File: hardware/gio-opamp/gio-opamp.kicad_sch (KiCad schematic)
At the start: 25 parts, among them J1 PJ3001F, J2 PJ3001F, U1 TL072, U2 MCP3208, U3 DAC8552, U4 XIAO-RP2350-DIP

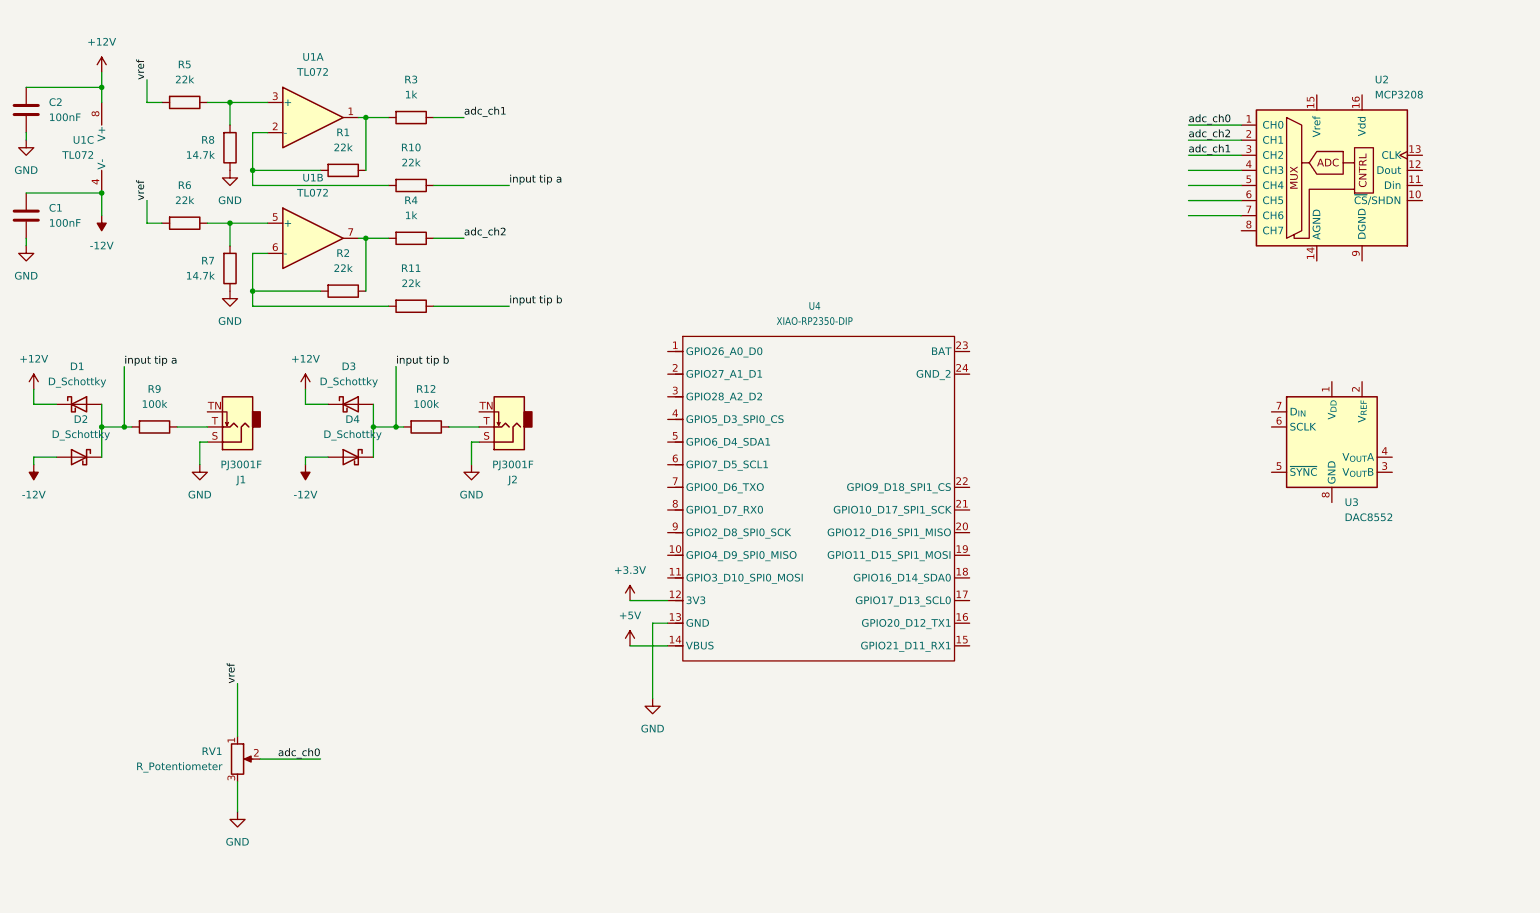
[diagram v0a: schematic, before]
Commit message: KiCad input stage: review-driven schematic refinements
Updates from the 2026-05-03 schematic review:

- Net `input tip a/b` renamed to `clamp_a/clamp_b` (more accurate --
  it's the protection node *after* R_series, not the jack tip itself).
- Local 100nF decoupling cap (C5) added directly across U1 V+/V- pins
  for fast op-amp transient response, in addition to the existing
  bulk caps on the +/-12V rails (C1/C2).
- Per-channel 100nF filter caps (C3/C4) on each bias-divider node to
  knock down any high-frequency noise riding on VREF before it reaches
  the op-amp non-inverting inputs.
- Schottky clamps switched from generic D_Schottky symbol to the
  BAT54S 3-pin series-pair (A=pin1, K=pin2, COM=pin3 on signal node).
  One part replaces two BAT43s per channel for the production PCB.

Schematic still input-stage-only; output stage / VREF / MCU coming
in subsequent edits.

Co-Authored-By: Claude Opus 4.7 (1M context) <noreply@anthropic.com>
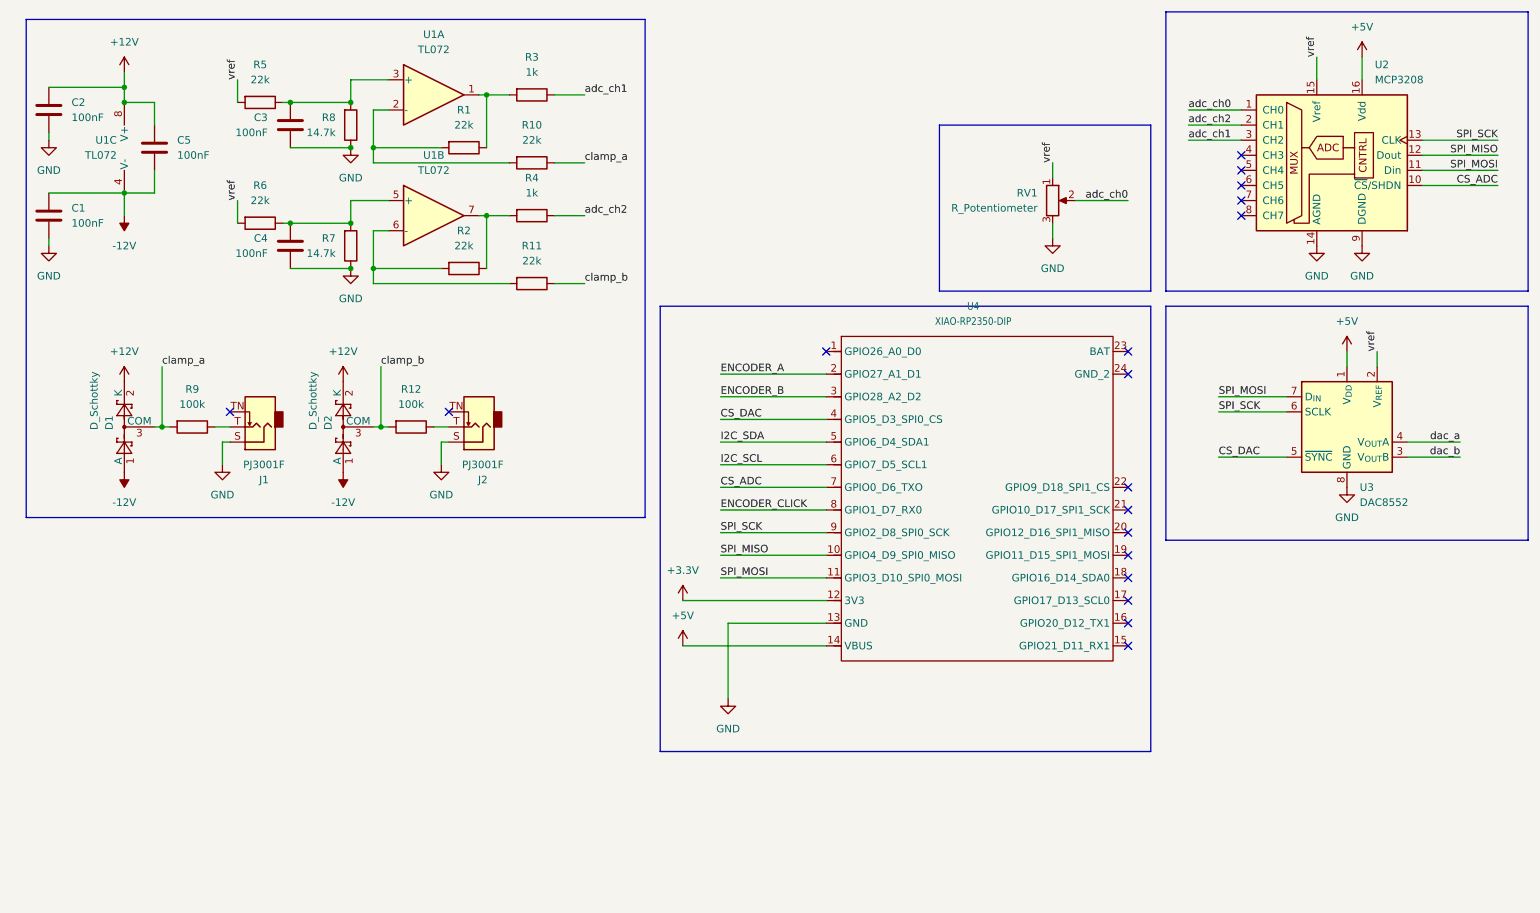
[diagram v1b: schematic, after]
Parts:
- removed D2, D3, D4: D_Schottky, symbol Device:D_Schottky
- added C3, C4, C5: 100nF, symbol Device:C
- added D2: D_Schottky, Package_TO_SOT_SMD:SOT-23, symbol Diode:BAT54S
- D1: footprint (none) -> Package_TO_SOT_SMD:SOT-23; symbol Device:D_Schottky -> Diode:BAT54S
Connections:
- net +12V: now also D1.2 (K), C5.1, D2.2 (K); no longer D1.1 (K)
- net +5V: now also U2.16 (Vdd), U3.1 (V_{DD})
- net -12V: now also D1.1 (A), C5.2, D2.1 (A)
- net GND: now also U2.14 (AGND), U2.9 (DGND), U3.8 (GND), C3.2, C4.2
- net vref: now also U2.15 (Vref), U3.2 (V_{REF})
- net at R6.1, R7.2, U1.5 (+): now also C4.1
- net at R5.1, R8.2, U1.3 (+): now also C3.1
- net SPI_MISO: now reaches U4.10 (GPIO4_D9_SPI0_MISO)
- net SPI_MISO: now also U2.12 (Dout)
- net SPI_MOSI: now reaches U4.11 (GPIO3_D10_SPI0_MOSI)
- net SPI_MOSI: now also U2.11 (Din), U3.7 (D_{IN})
- net ENCODER_A: now reaches U4.2 (GPIO27_A1_D1)
- net ENCODER_B: now reaches U4.3 (GPIO28_A2_D2)
- net CS_DAC: now reaches U4.4 (GPIO5_D3_SPI0_CS)
- net CS_DAC: now also U3.5 (~{SYNC})
- net I2C_SDA: now reaches U4.5 (GPIO6_D4_SDA1)
- net I2C_SCL: now reaches U4.6 (GPIO7_D5_SCL1)
- net CS_ADC: now reaches U4.7 (GPIO0_D6_TXO)
- net CS_ADC: now also U2.10 (~{CS}/SHDN)
- net ENCODER_CLICK: now reaches U4.8 (GPIO1_D7_RX0)
- net SPI_SCK: now reaches U4.9 (GPIO2_D8_SPI0_SCK)
- net SPI_SCK: now also U2.13 (CLK), U3.6 (SCLK)
- net dac_b: now reaches U3.3 (V_{OUT}B)
- net dac_a: now reaches U3.4 (V_{OUT}A)
- net input tip a renamed clamp_a
- net clamp_a: now also D1.3 (COM); no longer D1.2 (A)
- net input tip b renamed clamp_b
- net clamp_b: now also D2.3 (COM)
- no-connect marks 0 -> 18
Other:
- moved on the sheet: C1, C2, J1, R1, R10, R11, R2, R3, R4, R5, R6, R7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

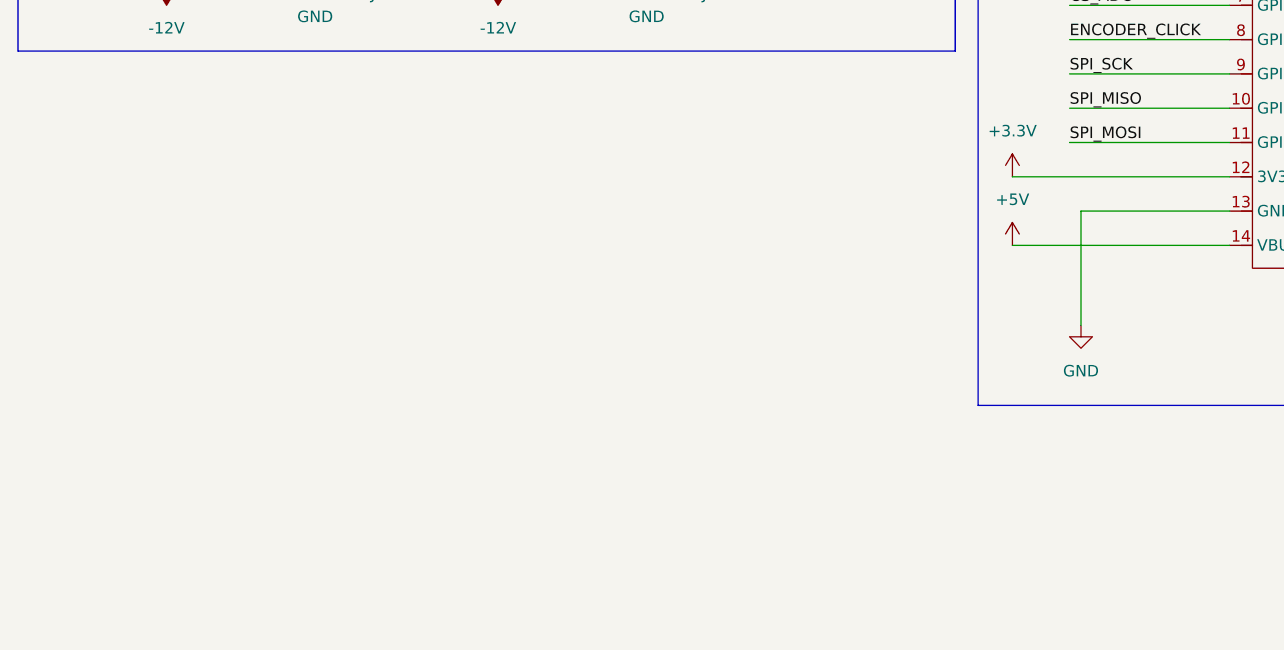
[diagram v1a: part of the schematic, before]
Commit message: KiCad: generate output op-amp stage (U5) via Python script
Adds the full output op-amp stage to the schematic by translating the
input op-amp section by +100 in Y and remapping references, values,
and net labels for the output topology.

Components added (all in y range 100-160 of the schematic):
  U5         TL072 (3 unit instances: U5A ch A, U5B ch B, U5C power)
  R13/R14    R_fb 47k (output gain 4.7 maps DAC 0..VREF -> jack +/-9V)
  R15/R16    R_jack_series 1k (output isolation before clamp/jack)
  R17/R18    R_off_top 22k (bias divider top, per channel)
  R19/R20    R_off_bot 14.7k (bias divider bottom)
  R21/R22    R_in 10k (DAC input resistor)
  C6/C7      bulk +/-12V decoupling
  C8/C9      bias-node 100nF filter caps
  C10        local V+/V- 100nF across U5 pins 4/8
  D3/D4      BAT54S clamps on jack tip (output overshoot protection)
  J3/J4      PJ3001F output jacks
  #PWR022-33 power flags (+12V, -12V, GND for new components)

Net labels:
  dac_a / dac_b -- DAC outputs feeding R_in
  out_a / out_b -- jack-tip nets after R_jack_series

Implementation:
  tools/gen-output-stage.py reads the existing schematic, finds all
  symbol/wire/junction/label blocks in the input op-amp's "common"
  zone (y in [20, 65]), translates them by +100 in Y, regenerates
  all UUIDs, remaps reference designators per a lookup table, and
  applies value overrides where the output topology differs (R_in
  22k -> 10k, R_fb 22k -> 47k). Then appends 20 fresh blocks for
  the output-side clamps, jacks, and connecting wires. The script
  is idempotent if rerun against the original schematic via the
  /tmp backup that gets created.

Validation done programmatically:
  - Paren balance verified (9226 open, 9226 close)
  - 538 unique UUIDs, zero duplicates
  - No designator collisions (U5 only references the new chip; pre-
    existing U2/U3/U4 were ADC/DAC/MCU)
  - All U5 pin positions have at least one wire connection
  - Project file used_designators updated (R1-22, C1-10, J1-4,
    D1-4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
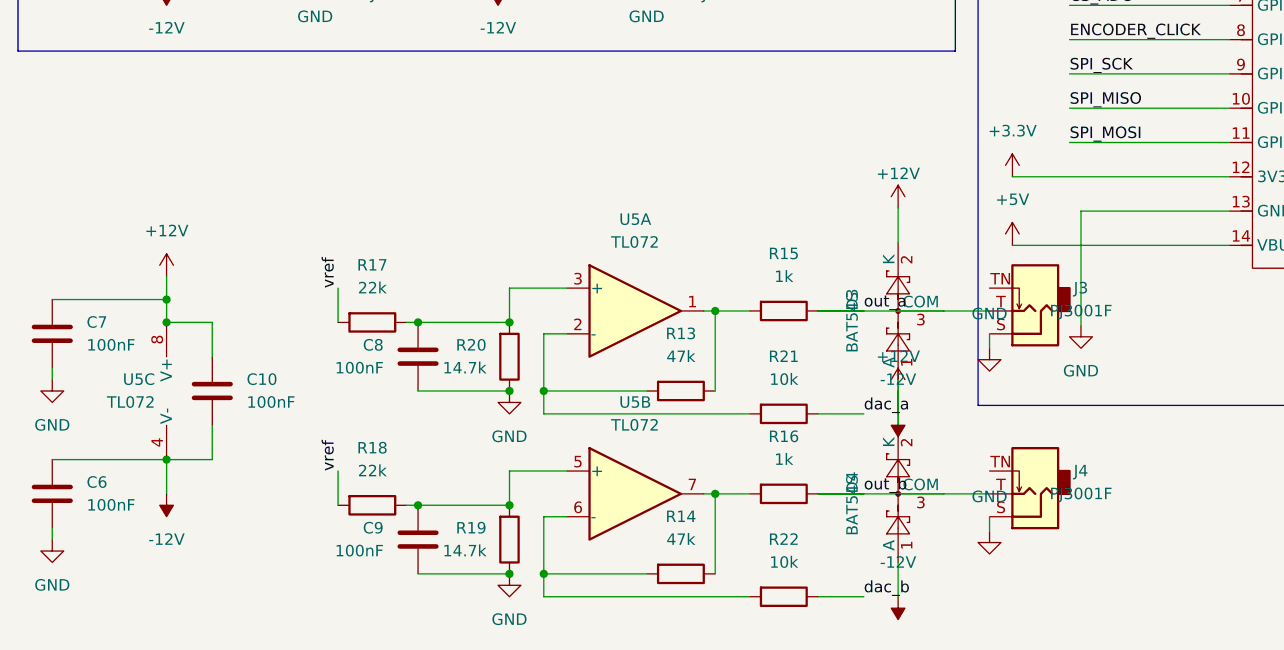
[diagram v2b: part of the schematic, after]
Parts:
- added C10, C6, C7, C8, C9: 100nF, symbol Device:C
- added D3, D4: BAT54S, symbol Diode:BAT54S
- added J3, J4: PJ3001F, symbol benjiaomodular:PJ3001F
- added R13, R14: 47k, symbol Device:R
- added R15, R16: 1k, symbol Device:R
- added R17, R18: 22k, symbol Device:R
- added R19, R20: 14.7k, symbol Device:R
- added R21, R22: 10k, symbol Device:R
- added U5: TL072, symbol Amplifier_Operational:TL072
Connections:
- net -12V is gone; now on net +12V: C1.1, C5.2, D1.1 (A), D2.1 (A), U1.4 (V-)
- net +12V: now also C10.1, C10.2, C6.1, C7.1, D3.1 (A), D3.2 (K), D4.1 (A), D4.2 (K), U5.4 (V-), U5.8 (V+)
- net GND: now also C6.2, C7.2, C8.2, C9.2, J3.S, J4.S, R19.1, R20.1
- net dac_a: now also R21.1
- net dac_b: now also R22.1
- net vref: now also R17.2, R18.2
- new net: R13.1, R15.2, U5.1
- new net: R14.2, R22.2, U5.6 (-)
- new net: C9.1, R18.1, R19.2, U5.5 (+)
- new net: C8.1, R17.1, R20.2, U5.3 (+)
- new net: R14.1, R16.2, U5.7
- new net: R13.2, R21.2, U5.2 (-)
- new net out_a: D3.3 (COM), J3.T, R15.1
- new net out_b: D4.3 (COM), J4.T, R16.1
